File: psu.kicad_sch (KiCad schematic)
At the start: 14 parts, among them J1 HRO_TYPE-C-31-M-14, J2 Battery, SW1 Battery, U2 ${ALTIUM_VALUE}

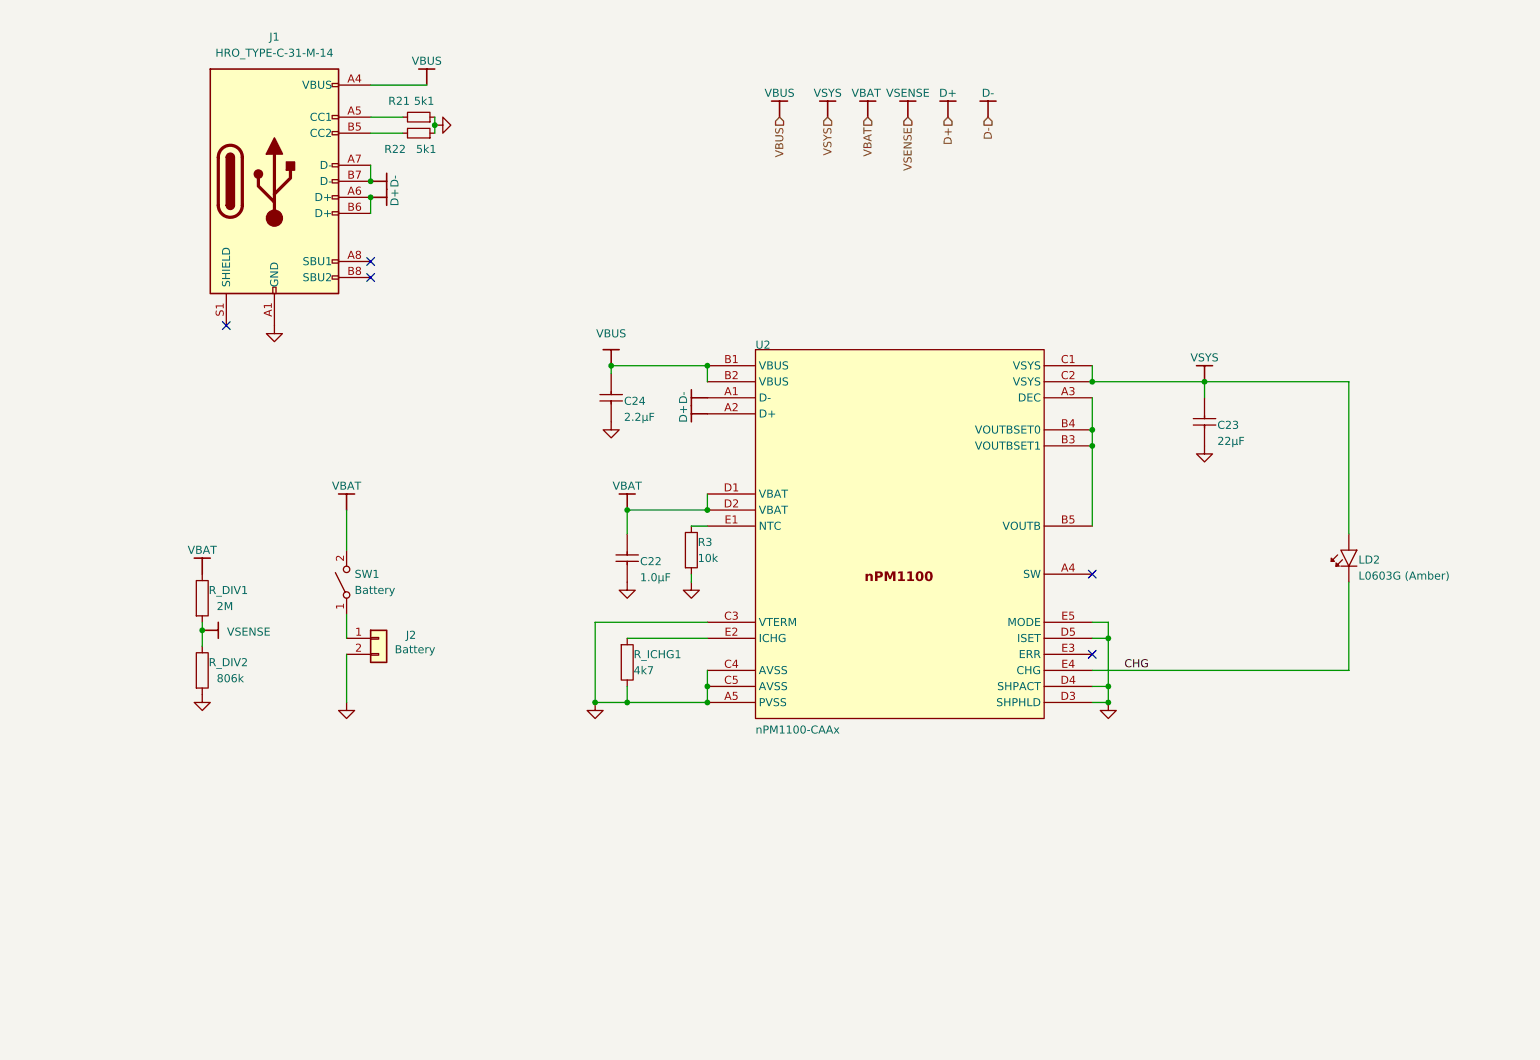
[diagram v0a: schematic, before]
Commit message: Reworking the PSU schematic to QDA package, adding DC/DC 1.8v source for optical sensor, and load switch for the battery sensor to prevent leakage
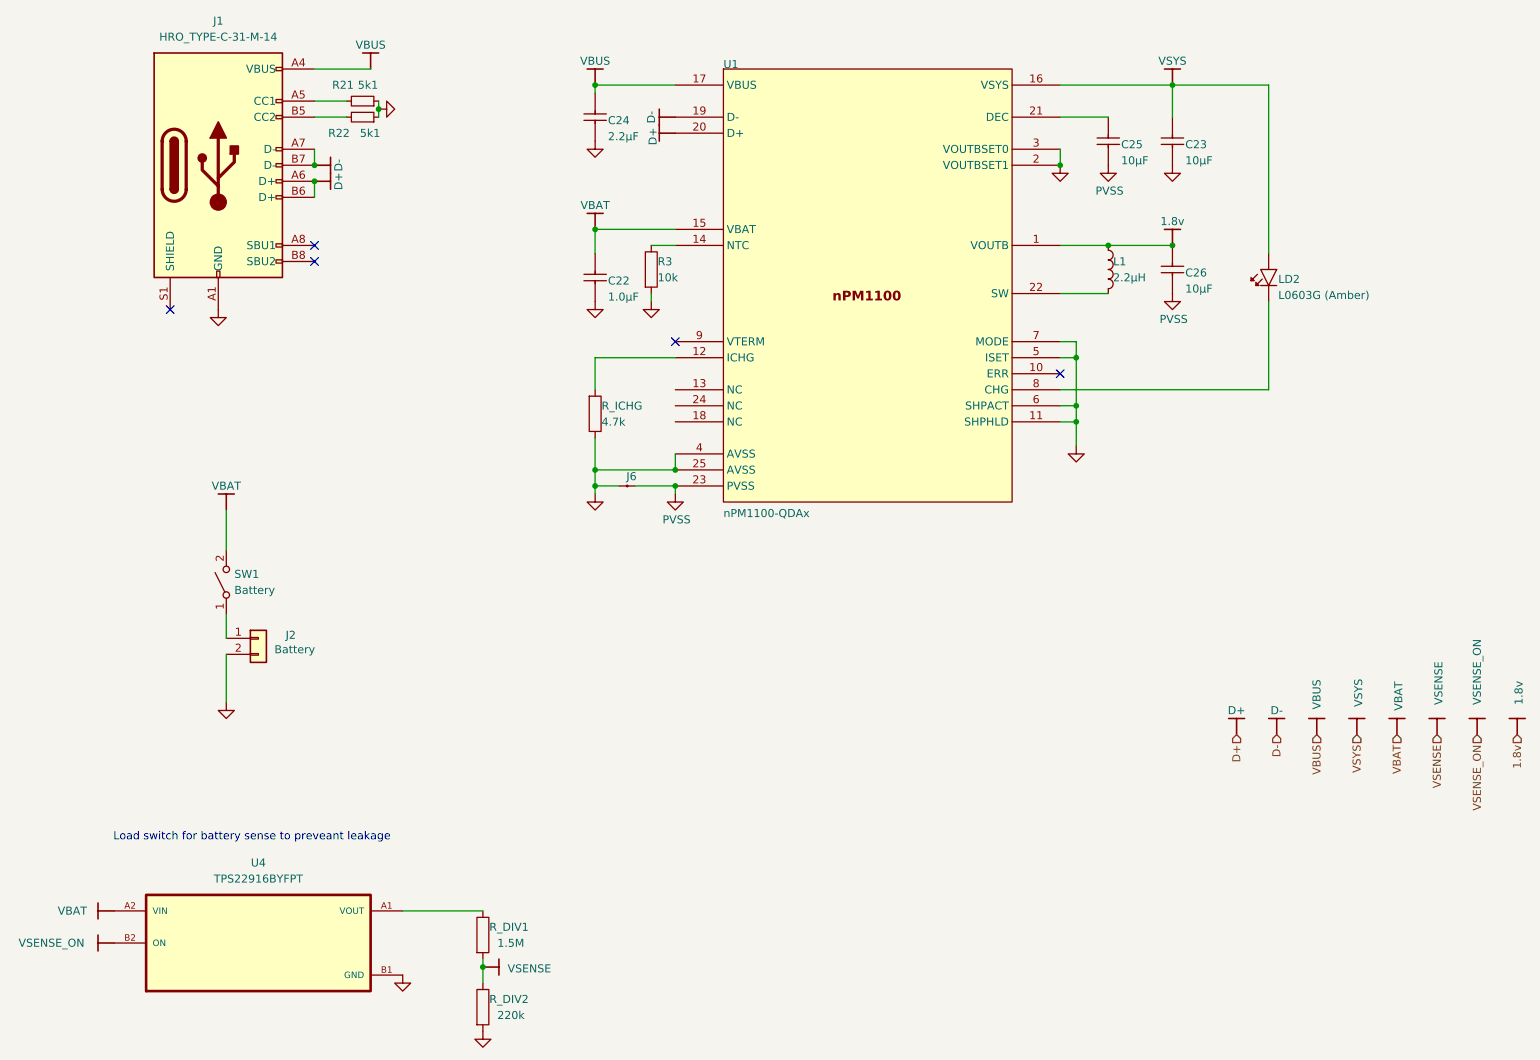
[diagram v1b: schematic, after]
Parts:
- removed R_ICHG1: ${ALTIUM_VALUE}, Resistor_SMD:R_0201_0603Metric, symbol AltiumLib:root_1_RES_AltiumLib.DbLib
- removed U2: ${ALTIUM_VALUE}, nRF Devices$:BGA25C40P5X5_200X200X50, symbol AltiumLib:root_0_nPM1100_CAAx_AltiumLib.DbLib
- added C25, C26: ${ALTIUM_VALUE}, CAPC1608X06L, symbol AltiumLib:root_1_CAP_AltiumLib.DbLib
- added J6: ${ALTIUM_VALUE}, 2 PIN STARPOINT, symbol AltiumLib:root_2_mirrored_2 pin starpoint_AltiumLib.DbLib
- added L1: ${ALTIUM_VALUE}, INDC2016X10N, symbol AltiumLib:root_3_IND_AltiumLib.DbLib
- added R_ICHG: 4.7k, RESC0603X03L_C, symbol AltiumLib:root_1_RES_AltiumLib.DbLib
- added U1: ${ALTIUM_VALUE}, QFN50P400X400X80_HS-25N, symbol AltiumLib:root_0_nPM1100_QDAx_AltiumLib.DbLib
- added U4: TPS22916BYFPT, TPS22916 load switch:BGA4C40P2X2_77X77X50, symbol TPS22916 load switch:TPS22916BYFPT
- C22: footprint Capacitor_SMD:C_0201_0603Metric -> CAPC0603X03L_C
- C23: footprint Capacitors$:CAPC1608X06L -> CAPC1608X06L; ALTIUM_VALUE 22µF -> 10µF
- C24: footprint Capacitors$:CAPC1608X06L -> CAPC1608X06L
- LD2: footprint LED_SMD:LED_0201_0603Metric -> LED_0603_G
- R_DIV1: value 2M -> 1.5M
- R_DIV2: value 806k -> 220k
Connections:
- net D+: now also U1.20 (D+)
- net D-: now also U1.19 (D-)
- net GND: now also J6.1, R_ICHG.1, U1.11 (SHPHLD), U1.2 (VOUTBSET1), U1.25 (AVSS), U1.3 (VOUTBSET0), U1.4 (AVSS), U1.5 (ISET), U1.6 (SHPACT), U1.7 (MODE), U4.B1 (GND)
- net VBAT: now also U1.15 (VBAT), U4.A2 (VIN); no longer R_DIV1.1
- net VBUS: now also U1.17 (VBUS)
- net VSYS: now also U1.16 (VSYS)
- net at R3.1: now also U1.14 (NTC)
- net CHG: no longer names the net of LD2.1 (C)
- net CHG: now also U1.8 (CHG)
- new net: R_ICHG.2, U1.12 (ICHG)
- new net: C25.2, U1.21 (DEC)
- new net: L1.2, U1.22 (SW)
- new net: R_DIV1.1, U4.A1 (VOUT)
- new net 1.8v: C26.2, L1.1, U1.1 (VOUTB)
- new net PVSS: C25.1, C26.1, J6.2, U1.23 (PVSS)
- new net VSENSE_ON: U4.B2 (ON)
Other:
- note added: "Load switch for battery sense to preveant leakage"
- moved on the sheet: J1, J2, R21, R22, R3, R_DIV1, R_DIV2, SW1

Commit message: Swapping the load switches from WLSP to WSON-6 packages
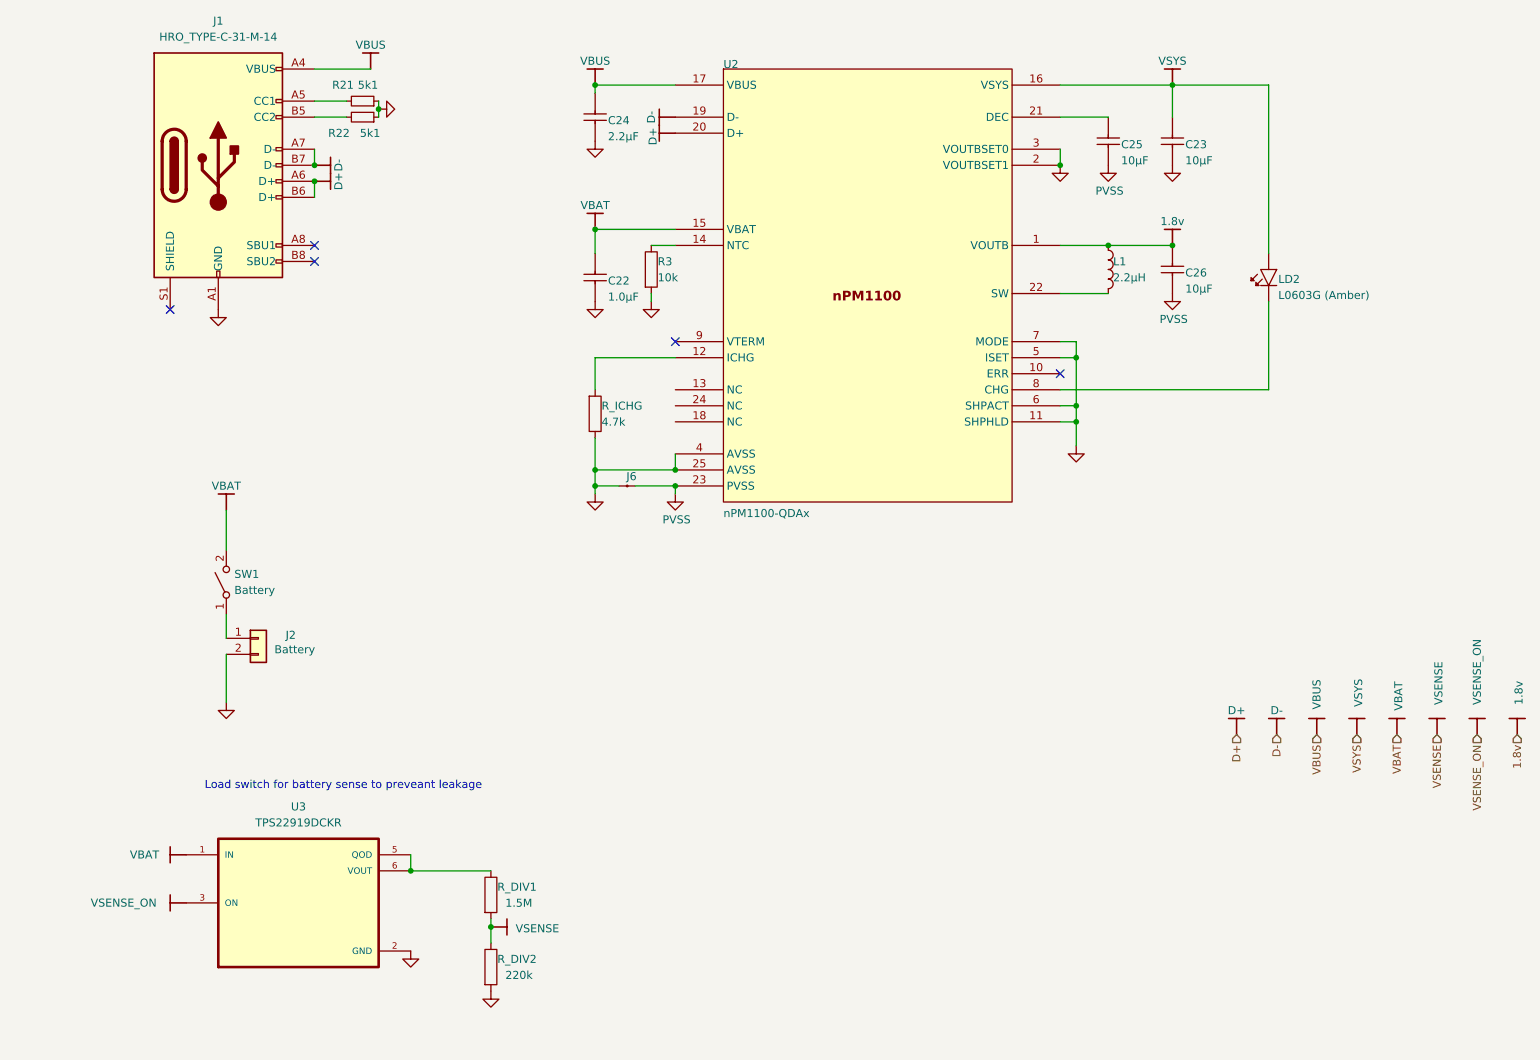
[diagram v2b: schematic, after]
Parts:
- removed U4: TPS22916BYFPT, TPS22916 load switch:BGA4C40P2X2_77X77X50, symbol TPS22916 load switch:TPS22916BYFPT
- added U3: TPS22919DCKR, TPS22919:SOT65P210X110-6N, symbol TPS22919:TPS22919DCKR
- renumbered U1 to U2
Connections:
- net GND: now also U3.2 (GND)
- net VBAT: now also U3.1 (IN)
- net VSENSE_ON: now also U3.3 (ON)
- net at R_DIV1.1: now also U3.5 (QOD), U3.6 (VOUT)
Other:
- moved on the sheet: R_DIV1, R_DIV2

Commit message: Cleaning up more components
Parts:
- renumbered L1 to L5
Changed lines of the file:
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@@
 		(on_board yes)
 		(dnp no)
-		(property "Reference" "L1"
+		(property "Reference" "L5"
 			(at 196.342 65.532 0)
 			(effects
@@
 			(project "plan-b"
 				(path "/3a835e6f-a660-4b38-a102-87841cdd95ed/9c2573bf-1407-4545-8610-25cf55ee3ffc"
-					(reference "L1")
+					(reference "L5")
 					(unit 1)
 				)

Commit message: Relinking the schematics and the PCB again
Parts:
- renumbered J6 to J99, R_ICHG to R_ICHG1
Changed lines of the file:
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@@
 		(on_board yes)
 		(dnp no)
-		(property "Reference" "#PWR?"
+		(property "Reference" "#PWR0109"
 			(at 205.74 62.23 0)
 			(effects
@@
 			(project "plan-b"
 				(path "/3a835e6f-a660-4b38-a102-87841cdd95ed/9c2573bf-1407-4545-8610-25cf55ee3ffc"
-					(reference "#PWR?")
+					(reference "#PWR0109")
 					(unit 1)
 				)
@@
 		(on_board yes)
 		(dnp no)
-		(property "Reference" "#PWR?"
+		(property "Reference" "#PWR0110"
 			(at 205.74 36.83 0)
 			(effects
@@
 			(project "plan-b"
 				(path "/3a835e6f-a660-4b38-a102-87841cdd95ed/9c2573bf-1407-4545-8610-25cf55ee3ffc"
-					(reference "#PWR?")
+					(reference "#PWR0110")
 					(unit 1)
 				)
@@
 		(on_board yes)
 		(dnp no)
-		(property "Reference" "#PWR?"
+		(property "Reference" "#PWR0112"
 			(at 114.3 59.69 0)
 			(effects
@@
 			(project "plan-b"
 				(path "/3a835e6f-a660-4b38-a102-87841cdd95ed/9c2573bf-1407-4545-8610-25cf55ee3ffc"
-					(reference "#PWR?")
+					(reference "#PWR0112")
 					(unit 1)
 				)
@@
 		(on_board yes)
 		(dnp no)
-		(property "Reference" "R_ICHG"
+		(property "Reference" "R_ICHG1"
 			(at 115.316 88.392 0)
 			(effects
@@
 			(project "plan-b"
 				(path "/3a835e6f-a660-4b38-a102-87841cdd95ed/9c2573bf-1407-4545-8610-25cf55ee3ffc"
-					(reference "R_ICHG")
+					(reference "R_ICHG1")
 					(unit 1)
 				)
@@
 		(on_board yes)
 		(dnp no)
-		(property "Reference" "J6"
+		(property "Reference" "J99"
 			(at 119.25 99.568 0)
 			(effects
@@
 			(project "plan-b"
 				(path "/3a835e6f-a660-4b38-a102-87841cdd95ed/9c2573bf-1407-4545-8610-25cf55ee3ffc"
-					(reference "J6")
+					(reference "J99")
 					(unit 1)
 				)
@@
 		(on_board yes)
 		(dnp no)
-		(property "Reference" "#PWR?"
+		(property "Reference" "#PWR0111"
 			(at 114.3 36.83 0)
 			(effects
@@
 			(project "plan-b"
 				(path "/3a835e6f-a660-4b38-a102-87841cdd95ed/9c2573bf-1407-4545-8610-25cf55ee3ffc"
-					(reference "#PWR?")
+					(reference "#PWR0111")
 					(unit 1)
 				)

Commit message: Tidying up the PSU block
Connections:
- no-connect marks 5 -> 8
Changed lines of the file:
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@@
+	)
+	(no_connect
+		(at 127 90.17)
 	)
 	(no_connect
@@
 	)
 	(no_connect
+		(at 127 87.63)
+	)
+	(no_connect
+		(at 127 85.09)
+	)
+	(no_connect

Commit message: Re-linking the PCB properties back to the schematics
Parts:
- C22: value ${ALTIUM_VALUE} -> 1.0µF; footprint CAPC0603X03L_C -> Library:C_0402_1005
- C23, C25, C26: value ${ALTIUM_VALUE} -> 10µF; footprint CAPC1608X06L -> Library:C_0603_1608
- C24: value ${ALTIUM_VALUE} -> 2.2µF; footprint CAPC1608X06L -> Library:C_0603_1608
- J99: value ${ALTIUM_VALUE} -> Net tie; footprint 2 PIN STARPOINT -> 2 pin starpoint:2 PIN STARPOINT
- L5: value ${ALTIUM_VALUE} -> 2.2µH; footprint INDC2016X10N -> Library:L_0603_1608
- LD2: footprint LED_0603_G -> Library:LED_0603_1608
- R21, R22, R_DIV1, R_DIV2: footprint Resistor_SMD:R_0201_0603Metric -> Library:R_0402_1005
- R3: value ${ALTIUM_VALUE} -> 10k; footprint Resistor_SMD:R_0201_0603Metric -> Library:R_0402_1005
- R_ICHG1: footprint RESC0603X03L_C -> Library:R_0402_1005
- U2: value ${ALTIUM_VALUE} -> nPM1100-QDAx; footprint QFN50P400X400X80_HS-25N -> Package_DFN_QFN:QFN-24-1EP_4x4mm_P0.5mm_EP2.6x2.6mm_ThermalVias; LATESTREVISIONDATE (none) -> 2017-08-21; PART NUMBER (none) -> nRF52840-QIAA; PUBLISHED (none) -> 2017-08-21
- U3: footprint TPS22919:SOT65P210X110-6N -> Package_TO_SOT_SMD:SOT-363_SC-70-6
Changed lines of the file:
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@@
 			)
 		)
-		(property "Value" "${ALTIUM_VALUE}"
+		(property "Value" "nPM1100-QDAx"
 			(at 134.62 105.41 0)
 			(effects
@@
 			)
 		)
-		(property "Footprint" "QFN50P400X400X80_HS-25N"
+		(property "Footprint" "Package_DFN_QFN:QFN-24-1EP_4x4mm_P0.5mm_EP2.6x2.6mm_ThermalVias"
 			(at 134.62 34.29 0)
 			(effects
@@
 			)
 		)
+		(property "LATESTREVISIONDATE" "2017-08-21"
+			(at 134.62 34.29 0)
+			(effects
+				(font
+					(size 1.27 1.27)
+				)
+				(hide yes)
+			)
+		)
+		(property "PART NUMBER" "nRF52840-QIAA"
+			(at 134.62 34.29 0)
+			(effects
+				(font
+					(size 1.27 1.27)
+				)
+				(hide yes)
+			)
+		)
+		(property "PUBLISHED" "2017-08-21"
+			(at 134.62 34.29 0)
+			(effects
+				(font
+					(size 1.27 1.27)
+				)
+				(hide yes)
+			)
+		)
 		(pin "8"
 		)
@@
 			)
 		)
-		(property "Footprint" "LED_0603_G"
+		(property "Footprint" "Library:LED_0603_1608"
 			(at 220.98 63.5 0)
 			(effects
@@
 			)
 		)
-		(property "Value" "${ALTIUM_VALUE}"
+		(property "Value" "1.0µF"
 			(at 116.332 71.12 0)
 			(effects
@@
 			)
 		)
-		(property "Footprint" "CAPC0603X03L_C"
+		(property "Footprint" "Library:C_0402_1005"
 			(at 114.3 71.12 0)
 			(effects
@@
 			)
 		)
-		(property "Value" "${ALTIUM_VALUE}"
+		(property "Value" "2.2µF"
 			(at 116.332 45.72 0)
 			(effects
@@
 			)
 		)
-		(property "Footprint" "CAPC1608X06L"
+		(property "Footprint" "Library:C_0603_1608"
 			(at 114.3 45.72 0)
 			(effects
@@
 			)
 		)
-		(property "Value" "${ALTIUM_VALUE}"
+		(property "Value" "10µF"
 			(at 207.772 49.53 0)
 			(effects
@@
 			)
 		)
-		(property "Footprint" "CAPC1608X06L"
+		(property "Footprint" "Library:C_0603_1608"
 			(at 205.74 49.53 0)
 			(effects
@@
 			)
 		)
-		(property "Value" "${ALTIUM_VALUE}"
+		(property "Value" "10µF"
 			(at 197.612 49.53 0)
 			(effects
@@
 			)
 		)
-		(property "Footprint" "CAPC1608X06L"
+		(property "Footprint" "Library:C_0603_1608"
 			(at 195.58 49.53 0)
 			(effects
@@
 			)
 		)
-		(property "Footprint" "Resistor_SMD:R_0201_0603Metric"
+		(property "Footprint" "Library:R_0402_1005"
 			(at 77.47 39.37 0)
 			(effects
@@
 			)
 		)
-		(property "Footprint" "RESC0603X03L_C"
+		(property "Footprint" "Library:R_0402_1005"
 			(at 114.3 92.71 0)
 			(effects
@@
 			)
 		)
-		(property "Footprint" "Resistor_SMD:R_0201_0603Metric"
+		(property "Footprint" "Library:R_0402_1005"
 			(at 97.79 161.29 0)
 			(effects
@@
 			)
 		)
-		(property "Footprint" "Resistor_SMD:R_0201_0603Metric"
+		(property "Footprint" "Library:R_0402_1005"
 			(at 97.79 172.72 0)
 			(effects
@@
 			)
 		)
-		(property "Value" "${ALTIUM_VALUE}"
+		(property "Value" "10k"
 			(at 124.206 68.072 0)
 			(effects
@@
 			)
 		)
-		(property "Footprint" "Resistor_SMD:R_0201_0603Metric"
+		(property "Footprint" "Library:R_0402_1005"
 			(at 123.19 62.23 0)
 			(effects
@@
 			)
 		)
+		(property "LCSC" ""
+			(at 123.19 62.23 0)
+			(effects
+				(font
+					(size 1.27 1.27)
+				)
+				(hide yes)
+			)
+		)
 		(pin "2"
 		)
@@
 			)
 		)
-		(property "Footprint" "TPS22919:SOT65P210X110-6N"
+		(property "Footprint" "Package_TO_SOT_SMD:SOT-363_SC-70-6"
 			(at 67.31 166.37 0)
 			(effects
@@
 			)
 		)
-		(property "Value" "${ALTIUM_VALUE}"
+		(property "Value" "Net tie"
 			(at 117.602 99.568 0)
 			(effects
@@
 			)
 		)
-		(property "Footprint" "2 PIN STARPOINT"
+		(property "Footprint" "2 pin starpoint:2 PIN STARPOINT"
 			(at 119.38 100.33 0)
 			(effects
@@
 			)
 		)
-		(property "Value" "${ALTIUM_VALUE}"
+		(property "Value" "10µF"
 			(at 207.772 69.85 0)
 			(effects
@@
 			)
 		)
-		(property "Footprint" "CAPC1608X06L"
+		(property "Footprint" "Library:C_0603_1608"
 			(at 205.74 69.85 0)
 			(effects
@@
 			)
 		)
-		(property "Value" "${ALTIUM_VALUE}"
+		(property "Value" "2.2µH"
 			(at 196.342 68.072 0)
 			(effects
@@
 			)
 		)
-		(property "Footprint" "INDC2016X10N"
+		(property "Footprint" "Library:L_0603_1608"
 			(at 195.58 62.23 0)
 			(effects
@@
 			)
 		)
-		(property "Footprint" "Resistor_SMD:R_0201_0603Metric"
+		(property "Footprint" "Library:R_0402_1005"
 			(at 77.47 41.91 0)
 			(effects

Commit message: Reworking the PSU block and squeeshing everything into 16x42mm space
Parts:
- removed C23: 10µF, Library:C_0603_1608, symbol AltiumLib:root_1_CAP_AltiumLib.DbLib
- removed C24: 2.2µF, Library:C_0603_1608, symbol AltiumLib:root_1_CAP_AltiumLib.DbLib

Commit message: Optimising for BOM and placements cost reduction
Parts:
- J1: value HRO_TYPE-C-31-M-14 -> HRO_TYPE-C-31-M-12
- J99: now left out of the parts list
- R_DIV1: value 1.5M -> 100k
- R_DIV2: value 220k -> 100k
- R_ICHG1: value 4.7k -> 5k1
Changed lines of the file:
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@@
 			)
 		)
-		(property "Value" "HRO_TYPE-C-31-M-14"
+		(property "Value" "HRO_TYPE-C-31-M-12"
 			(at 54.61 29.21 0)
 			(effects
@@
 			)
 		)
-		(property "Value" "4.7k"
+		(property "Value" "5k1"
 			(at 115.316 90.932 0)
 			(effects
@@
 			)
 		)
-		(property "Value" "1.5M"
+		(property "Value" "100k"
 			(at 100.076 167.132 0)
 			(effects
@@
 			)
 		)
-		(property "Value" "220k"
+		(property "Value" "100k"
 			(at 100.076 178.562 0)
 			(effects
@@
 		(unit 1)
 		(exclude_from_sim no)
-		(in_bom yes)
-		(on_board yes)
-		(dnp no)
+		(in_bom no)
+		(on_board yes)
+		(dnp no)
